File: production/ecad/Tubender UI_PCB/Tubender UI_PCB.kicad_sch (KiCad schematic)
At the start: 0 parts

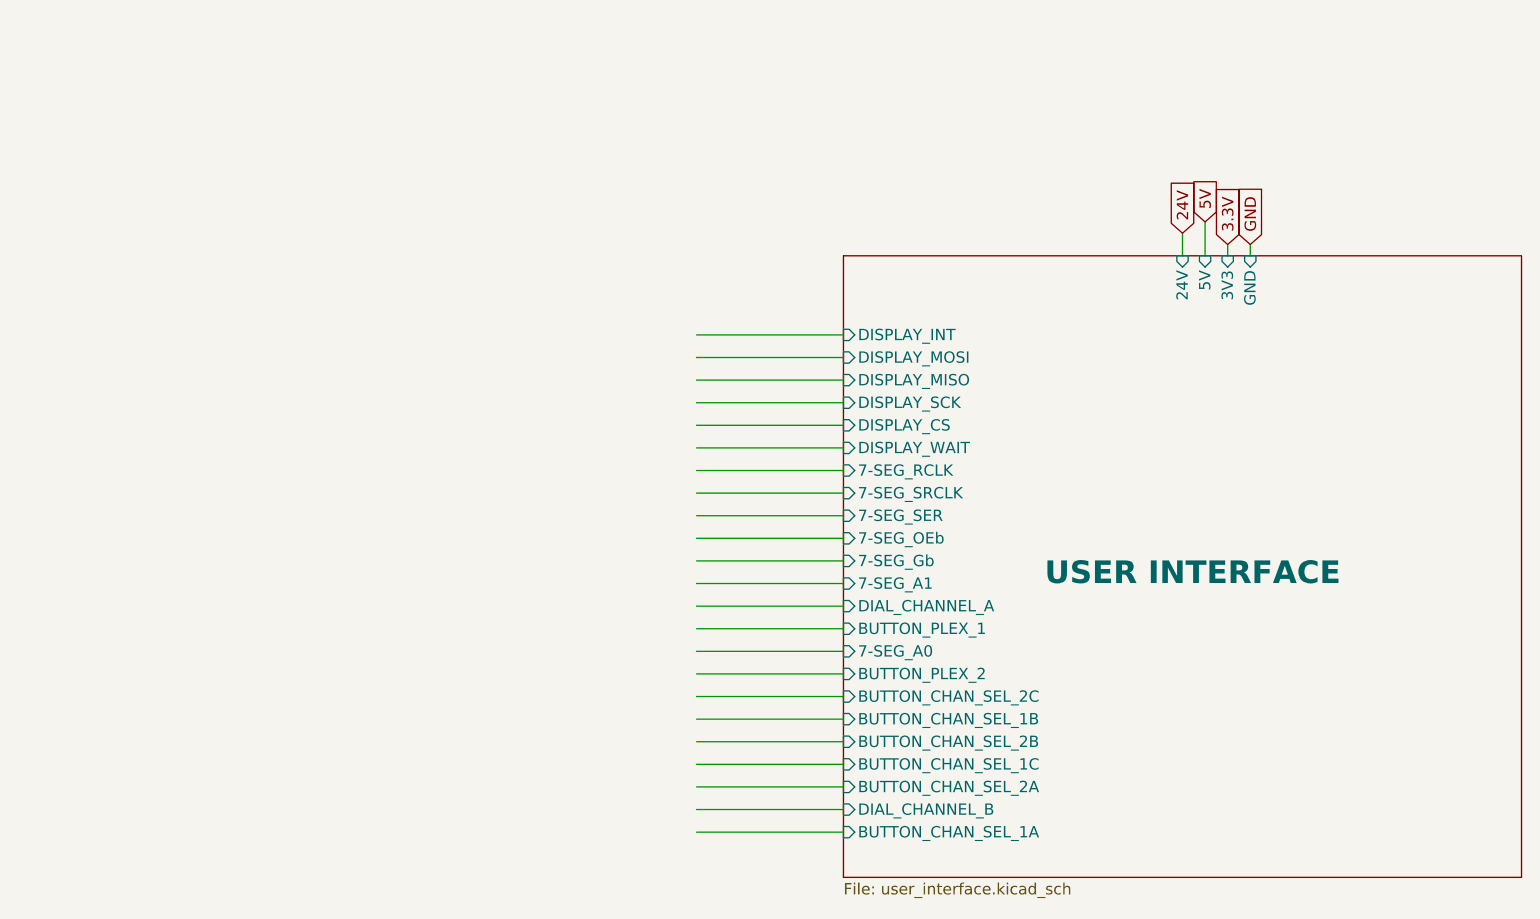
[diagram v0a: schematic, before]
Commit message: UI Board Fully Separated Now
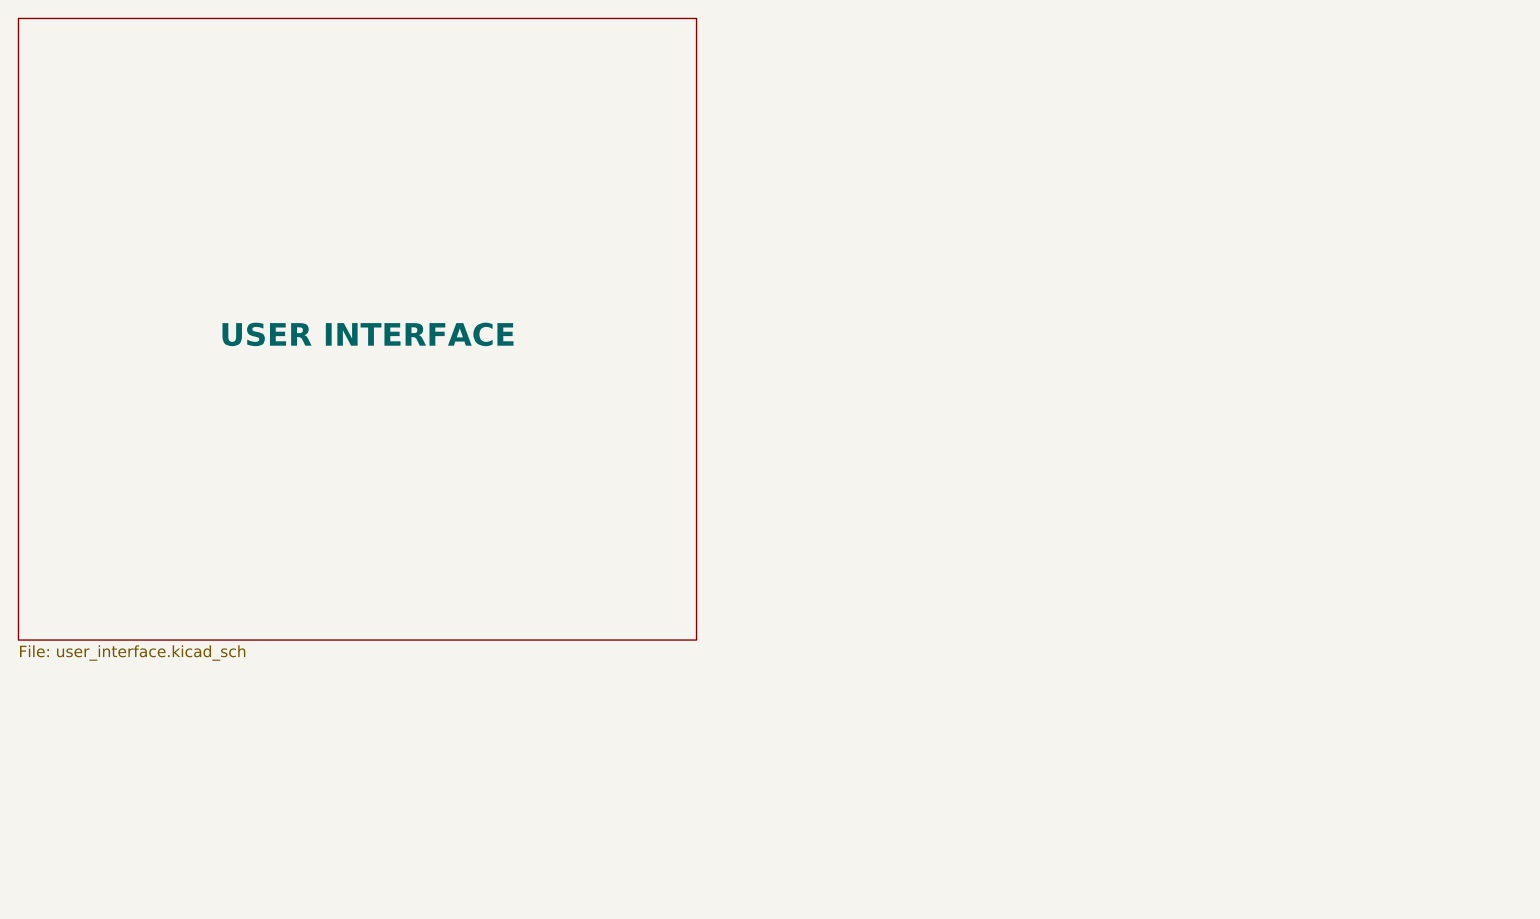
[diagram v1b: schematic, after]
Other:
- sheet USER INTERFACE ports: added none; removed 24V, 3V3, 5V, 7-SEG_A0, 7-SEG_A1, 7-SEG_Gb, 7-SEG_OEb, 7-SEG_RCLK, 7-SEG_SER, 7-SEG_SRCLK, BUTTON_CHAN_SEL_1A, BUTTON_CHAN_SEL_1B, BUTTON_CHAN_SEL_1C, BUTTON_CHAN_SEL_2A, BUTTON_CHAN_SEL_2B, BUTTON_CHAN_SEL_2C, BUTTON_PLEX_1, BUTTON_PLEX_2, DIAL_CHANNEL_A, DIAL_CHANNEL_B, DISPLAY_CS, DISPLAY_INT, DISPLAY_MISO, DISPLAY_MOSI, DISPLAY_SCK, DISPLAY_WAIT, GND
